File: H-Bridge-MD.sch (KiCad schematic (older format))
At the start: 69 parts, among them IC1 SI8650AB-B-IS1, IC2 A3921KLPTR-T, IC3 SI8650AB-B-IS1, IC4 A3921KLPTR-T, J1 Conn_01x02, J2 Conn_01x03, J3 Conn_01x05, J4 Conn_01x02, J5 Bus_mechaken_PCIexpress_x16_1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, Q1 NVMFD5C446NT1G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

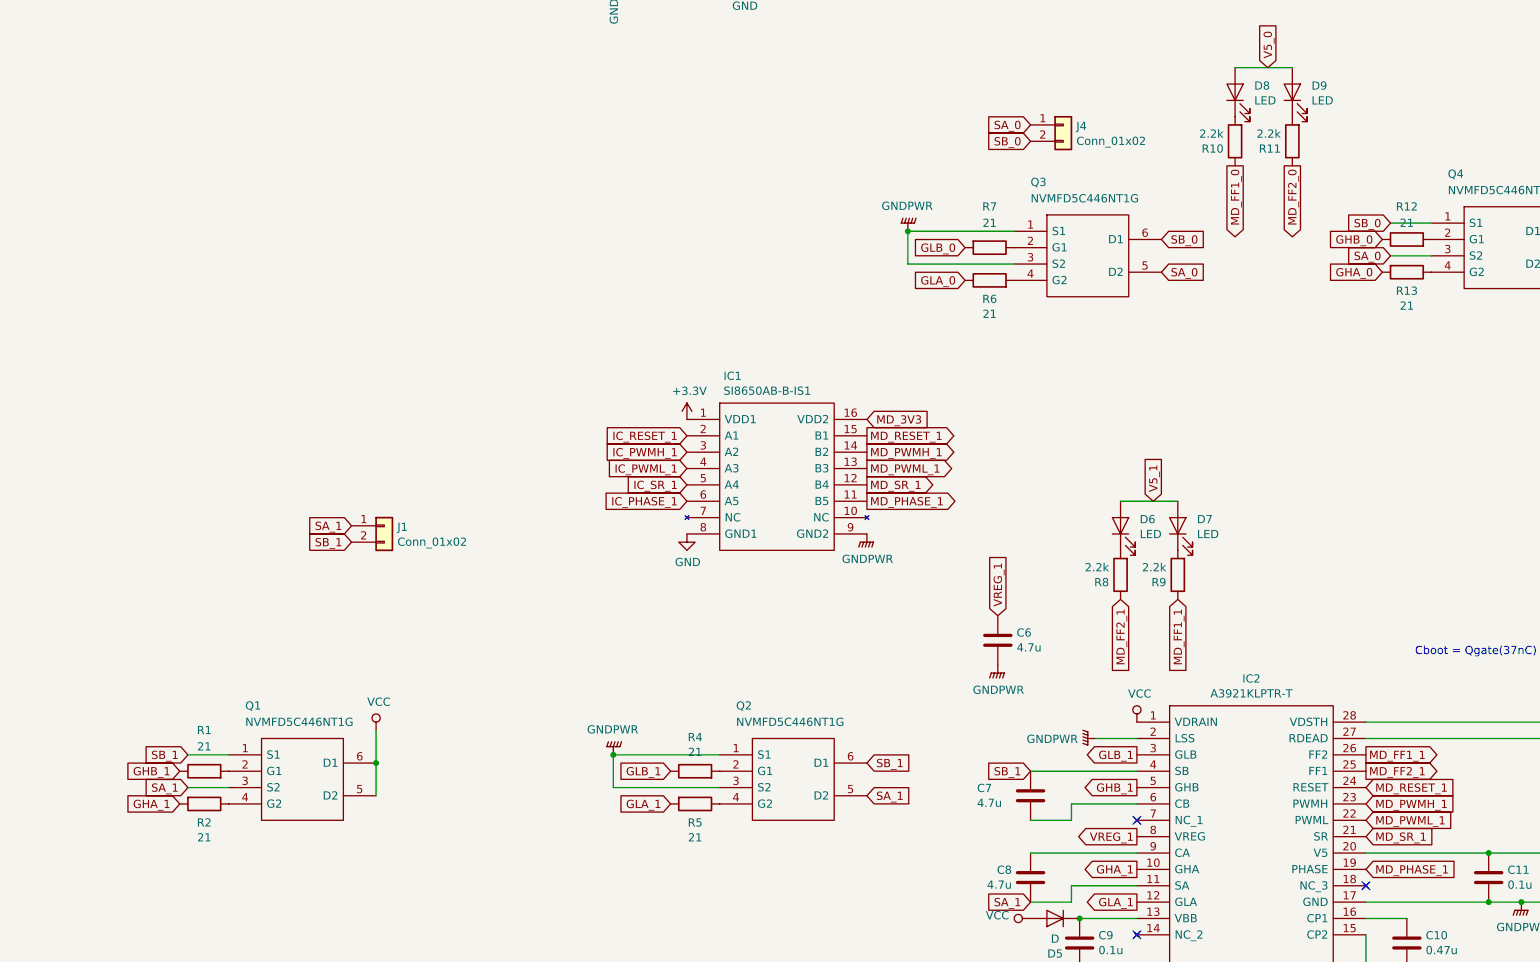
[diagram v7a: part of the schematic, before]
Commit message: change
FET等の裏表反転
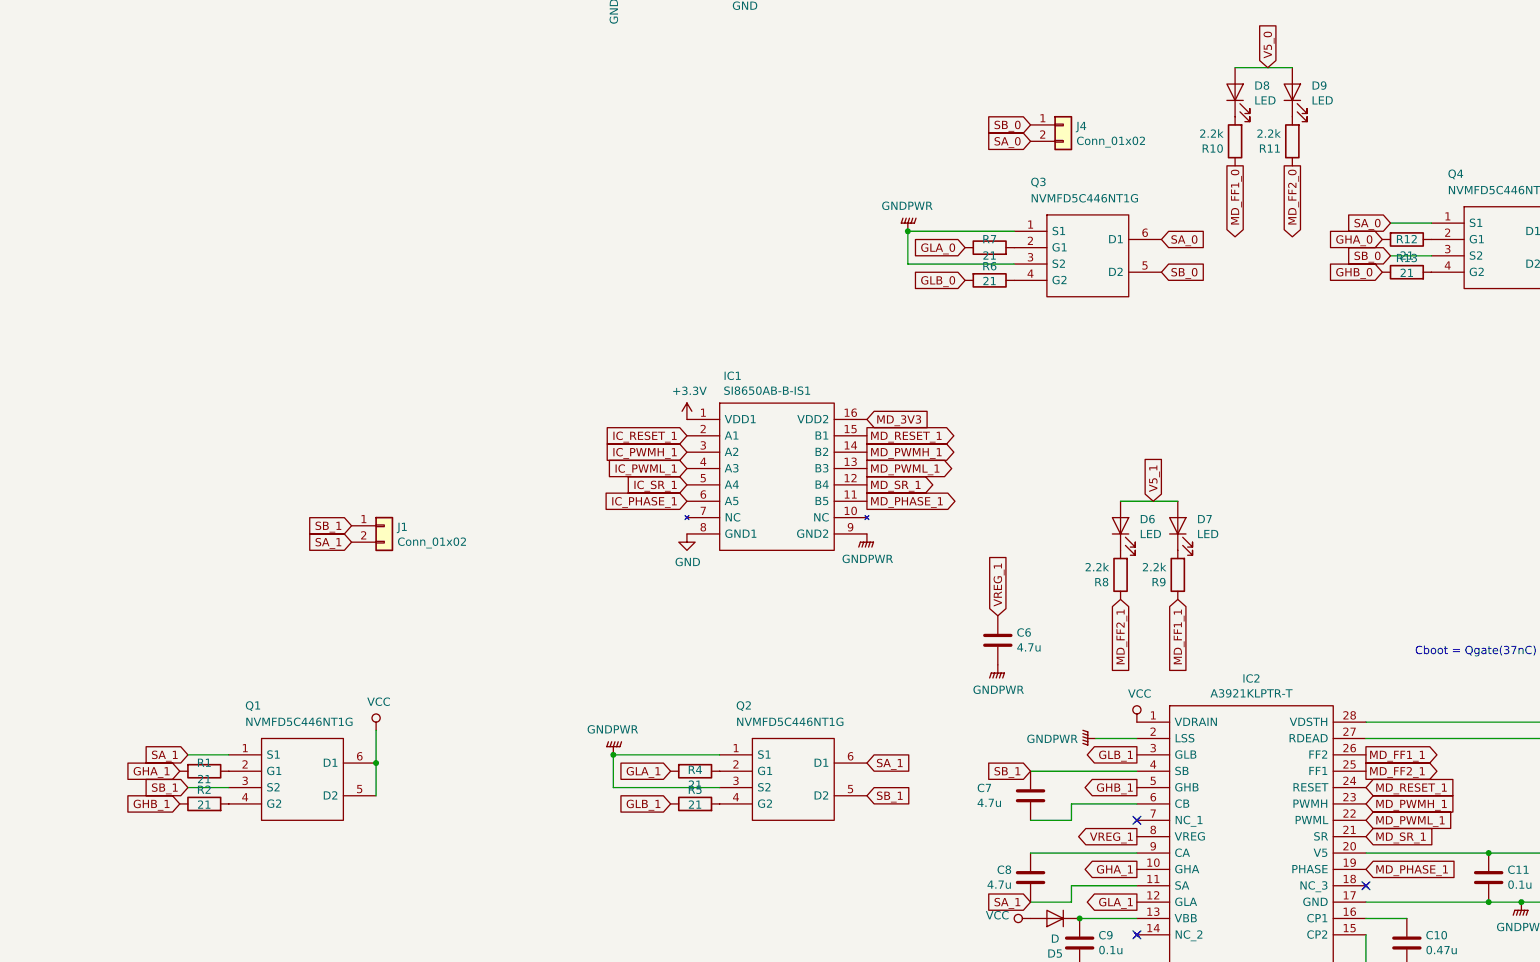
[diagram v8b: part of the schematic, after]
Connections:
- net SA_0: now also J4.2 (Pin_2), Q3.6 (D1), Q4.1 (S1); no longer J4.1 (Pin_1), Q3.5 (D2), Q4.3 (S2)
- net SA_1: now also J1.2 (Pin_2), Q1.1 (S1), Q2.6 (D1); no longer J1.1 (Pin_1), Q1.3 (S2), Q2.5 (D2)
- net SB_0: now also J4.1 (Pin_1), Q3.5 (D2), Q4.3 (S2); no longer J4.2 (Pin_2), Q3.6 (D1), Q4.1 (S1)
- net SB_1: now also J1.1 (Pin_1), Q1.3 (S2), Q2.5 (D2); no longer J1.2 (Pin_2), Q1.1 (S1), Q2.6 (D1)
- net at R4.2: now also Q2.4 (G2); no longer Q2.2 (G1)
- net at R1.2: now also Q1.4 (G2); no longer Q1.2 (G1)
- net at R5.1: now also Q2.2 (G1); no longer Q2.4 (G2)
- net at R2.1: now also Q1.2 (G1); no longer Q1.4 (G2)
- net at R6.2: now also Q3.2 (G1); no longer Q3.4 (G2)
- net at R12.2: now also Q4.4 (G2); no longer Q4.2 (G1)
- net at R13.1: now also Q4.2 (G1); no longer Q4.4 (G2)
- net at R7.1: now also Q3.4 (G2); no longer Q3.2 (G1)
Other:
- moved on the sheet: R1, R12, R13, R2, R4, R5, R6, R7
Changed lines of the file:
@@
 	1    0    0    -1
 $EndComp
+Text GLabel 2900 8100 0    50   Input ~ 0
+SB_1
 Text GLabel 2900 8200 0    50   Input ~ 0
-SB_1
-Text GLabel 2900 8100 0    50   Input ~ 0
 SA_1
-Text GLabel 6050 9550 2    50   Input ~ 0
+Text GLabel 6050 9750 2    50   Input ~ 0
 SB_1
 $Comp
@@
 Text GLabel 7700 10400 0    50   Output ~ 0
 GLA_1
-Text GLabel 6050 9750 2    50   Input ~ 0
+Text GLabel 6050 9550 2    50   Input ~ 0
 SA_1
 Text GLabel 7050 9600 0    50   Input ~ 0
@@
 Text GLabel 7050 10400 0    50   Input ~ 0
 SA_1
+Text GLabel 1900 9700 0    50   Input ~ 0
+SB_1
 Text GLabel 1900 9500 0    50   Input ~ 0
-SB_1
-Text GLabel 1900 9700 0    50   Input ~ 0
 SA_1
 $Comp
@@
 	1    0    0    -1
 $EndComp
+Text GLabel 1850 9600 0    50   Input ~ 0
+GHA_1
 Text GLabel 1850 9800 0    50   Input ~ 0
-GHA_1
-Text GLabel 1850 9600 0    50   Input ~ 0
 GHB_1
 Text GLabel 7700 10200 0    50   Output ~ 0
@@
 L Device:R R2
 U 1 1 5DA97C08
+P 2000 9600
+F 0 "R2" V 2115 9600 50  0000 C CNN
+F 1 "21" V 2206 9600 50  0000 C CNN
+F 2 "Resistor_SMD:R_0603_1608Metric" V 1930 9600 50  0001 C CNN
+F 3 "~" H 2000 9600 50  0001 C CNN
+	1    2000 9600
+	0    1    1    0
+$EndComp
+$Comp
+L Device:R R1
+U 1 1 5DA97BF0
 P 2000 9800
-F 0 "R2" V 2115 9800 50  0000 C CNN
-F 1 "21" V 2206 9800 50  0000 C CNN
+F 0 "R1" V 2250 9800 50  0000 C CNN
+F 1 "21" V 2150 9800 50  0000 C CNN
 F 2 "Resistor_SMD:R_0603_1608Metric" V 1930 9800 50  0001 C CNN
 F 3 "~" H 2000 9800 50  0001 C CNN
 	1    2000 9800
-	0    1    1    0
-$EndComp
-$Comp
-L Device:R R1
-U 1 1 5DA97BF0
-P 2000 9600
-F 0 "R1" V 2250 9600 50  0000 C CNN
-F 1 "21" V 2150 9600 50  0000 C CNN
-F 2 "Resistor_SMD:R_0603_1608Metric" V 1930 9600 50  0001 C CNN
-F 3 "~" H 2000 9600 50  0001 C CNN
-	1    2000 9600
 	0    -1   -1   0
 $EndComp
@@
 	4200 2900 5300 2900
 Connection ~ 5300 4750
-Text GLabel 6650 6600 0    50   Input ~ 0
+Text GLabel 6650 6400 0    50   Input ~ 0
 GLA_0
 Connection ~ 6300 6300
@@
 L Device:R R12
 U 1 1 5DC02421
+P 9350 6550
+F 0 "R12" V 9550 6550 50  0000 C CNN
+F 1 "21" V 9450 6550 50  0000 C CNN
+F 2 "Resistor_SMD:R_0603_1608Metric" V 9280 6550 50  0001 C CNN
+F 3 "~" H 9350 6550 50  0001 C CNN
+	1    9350 6550
+	0    -1   -1   0
+$EndComp
+$Comp
+L Device:R R13
+U 1 1 5DC02427
 P 9350 6350
-F 0 "R12" V 9550 6350 50  0000 C CNN
-F 1 "21" V 9450 6350 50  0000 C CNN
+F 0 "R13" V 9465 6350 50  0000 C CNN
+F 1 "21" V 9556 6350 50  0000 C CNN
 F 2 "Resistor_SMD:R_0603_1608Metric" V 9280 6350 50  0001 C CNN
 F 3 "~" H 9350 6350 50  0001 C CNN
 	1    9350 6350
-	0    -1   -1   0
-$EndComp
-$Comp
-L Device:R R13
-U 1 1 5DC02427
-P 9350 6550
-F 0 "R13" V 9465 6550 50  0000 C CNN
-F 1 "21" V 9556 6550 50  0000 C CNN
-F 2 "Resistor_SMD:R_0603_1608Metric" V 9280 6550 50  0001 C CNN
-F 3 "~" H 9350 6550 50  0001 C CNN
-	1    9350 6550
 	0    1    1    0
 $EndComp
+Text GLabel 9200 6550 0    50   Input ~ 0
+GHB_0
 Text GLabel 9200 6350 0    50   Input ~ 0
-GHB_0
-Text GLabel 9200 6550 0    50   Input ~ 0
 GHA_0
 $Comp
@@
 	1    0    0    -1
 $EndComp
+Text GLabel 9250 6250 0    50   Input ~ 0
+SA_0
 Text GLabel 9250 6450 0    50   Input ~ 0
-SA_0
-Text GLabel 9250 6250 0    50   Input ~ 0
 SB_0
 Text GLabel 11250 6850 0    50   Input ~ 0
@@
 	1    0    0    -1
 $EndComp
-Text GLabel 6650 6400 0    50   Input ~ 0
+Text GLabel 6650 6600 0    50   Input ~ 0
 GLB_0
 $Comp
 L Device:R R7
 U 1 1 5DC02488
-P 6800 6400
-F 0 "R7" V 6550 6400 50  0000 C CNN
-F 1 "21" V 6650 6400 50  0000 C CNN
-F 2 "Resistor_SMD:R_0603_1608Metric" V 6730 6400 50  0001 C CNN
-F 3 "~" H 6800 6400 50  0001 C CNN
-	1    6800 6400
+P 6800 6600
+F 0 "R7" V 6550 6600 50  0000 C CNN
+F 1 "21" V 6650 6600 50  0000 C CNN
+F 2 "Resistor_SMD:R_0603_1608Metric" V 6730 6600 50  0001 C CNN
+F 3 "~" H 6800 6600 50  0001 C CNN
+	1    6800 6600
 	0    1    1    0
 $EndComp
@@
 Wire Wire Line
 	6300 6500 6300 6300
+Text GLabel 7050 5750 0    50   Input ~ 0
+SA_0
 Text GLabel 7050 5650 0    50   Input ~ 0
-SA_0
-Text GLabel 7050 5750 0    50   Input ~ 0
 SB_0
 $Comp
@@
 	5450 3000 5450 3300
 Wire Wire Line
+	9250 6450 9500 6450
+Wire Wire Line
 	9250 6250 9500 6250
 Wire Wire Line
-	9250 6450 9500 6450
-Wire Wire Line
 	4500 9700 5150 9700
 Wire Wire Line
 	4500 9500 5150 9500
-$Comp
-L Device:R R4
-U 1 1 5DA97BEA
-P 5000 9600
-F 0 "R4" V 5207 9600 50  0000 C CNN
-F 1 "21" V 5116 9600 50  0000 C CNN
-F 2 "Resistor_SMD:R_0603_1608Metric" V 4930 9600 50  0001 C CNN
-F 3 "~" H 5000 9600 50  0001 C CNN
-	1    5000 9600
-	0    -1   -1   0
-$EndComp
-Text GLabel 4850 9800 0    50   Input ~ 0
-GLA_1
-Text GLabel 4850 9600 0    50   Input ~ 0
-GLB_1
-$Comp
-L Device:R R5
-U 1 1 5DA97C02
-P 5000 9800
-F 0 "R5" V 5115 9800 50  0000 C CNN
-F 1 "21" V 5206 9800 50  0000 C CNN
-F 2 "Resistor_SMD:R_0603_1608Metric" V 4930 9800 50  0001 C CNN
-F 3 "~" H 5000 9800 50  0001 C CNN
-	1    5000 9800
-	0    1    1    0
-$EndComp
 $Comp
 L power:GNDPWR #PWR015
@@
 	1    0    0    -1
 $EndComp
-Text GLabel 7850 6550 2    50   Input ~ 0
+Text GLabel 7850 6350 2    50   Input ~ 0
 SA_0
 $Comp
@@
 	1    0    0    -1
 $EndComp
-Text GLabel 7850 6350 2    50   Input ~ 0
+Text GLabel 7850 6550 2    50   Input ~ 0
 SB_0
 $Comp
@@
 L Device:R R6
 U 1 1 5DC0241B
-P 6800 6600
-F 0 "R6" V 6685 6600 50  0000 C CNN
-F 1 "21" V 6594 6600 50  0000 C CNN
-F 2 "Resistor_SMD:R_0603_1608Metric" V 6730 6600 50  0001 C CNN
-F 3 "~" H 6800 6600 50  0001 C CNN
-	1    6800 6600
+P 6800 6400
+F 0 "R6" V 6685 6400 50  0000 C CNN
+F 1 "21" V 6594 6400 50  0000 C CNN
+F 2 "Resistor_SMD:R_0603_1608Metric" V 6730 6400 50  0001 C CNN
+F 3 "~" H 6800 6400 50  0001 C CNN
+	1    6800 6400
 	0    -1   -1   0
 $EndComp
@@
 Text GLabel 6300 1900 0    50   Output ~ 0
 DIP_SW_4
+$Comp
+L Device:R R5
+U 1 1 5DA97C02
+P 5000 9600
+F 0 "R5" V 5115 9600 50  0000 C CNN
+F 1 "21" V 5206 9600 50  0000 C CNN
+F 2 "Resistor_SMD:R_0603_1608Metric" V 4930 9600 50  0001 C CNN
+F 3 "~" H 5000 9600 50  0001 C CNN
+	1    5000 9600
+	0    1    1    0
+$EndComp
+Text GLabel 4850 9600 0    50   Input ~ 0
+GLA_1
+Text GLabel 4850 9800 0    50   Input ~ 0
+GLB_1
+$Comp
+L Device:R R4
+U 1 1 5DA97BEA
+P 5000 9800
+F 0 "R4" V 5207 9800 50  0000 C CNN
+F 1 "21" V 5116 9800 50  0000 C CNN
+F 2 "Resistor_SMD:R_0603_1608Metric" V 4930 9800 50  0001 C CNN
+F 3 "~" H 5000 9800 50  0001 C CNN
+	1    5000 9800
+	0    -1   -1   0
+$EndComp
 $EndSCHEMATC
